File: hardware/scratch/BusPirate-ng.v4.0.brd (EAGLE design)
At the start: 100 x 50 mm, 136 parts, among them CON1 CON-USB-F-MICRO-B, IC10 74LVC1G07DBV, IC11 IC_BUFF_SN74LVC1T45DBV, IC12 74LVC1G07DBV, IC13 IC_BUFF_SN74LVC1T45DBV, IC14 74LVC1G07DBV, IC15 IC_BUFF_SN74LVC1T45DBV, IC16 74LVC1G07DBV, IC17 IC_BUFF_SN74LVC1T45DBV, IC2 IC_MEM_23LC1024, IC3 IC_MEM_23LC1024, IC4 IC_74AC573, IC5 IC_BL1551, IC6 IC_BL1551, IC7 74HCT4066PW, IC8 74LVC1G07DBV, IC9 IC_BUFF_SN74LVC1T45DBV, J1 CON_HEADER_1X04, J2 CON_HEADER_1X03-PTH, J3 CON_HEADER_2X02-PTH, J5 CON_HEADER_1X10-RIGHT_ANGLED_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, U1 IC_FPGA_ICE40HX4K, U2 IC_UC_STM32F103ZX, U3 IC_MEM_AT45DB041D

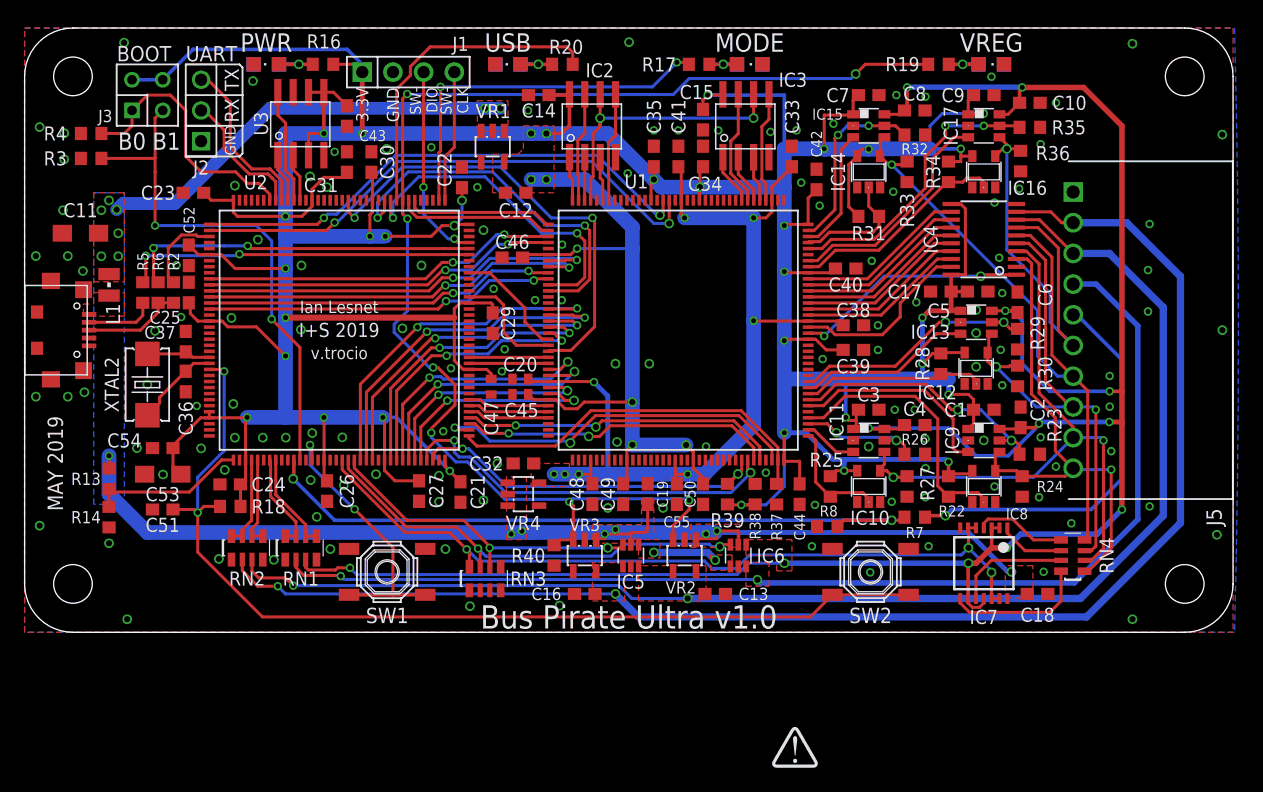
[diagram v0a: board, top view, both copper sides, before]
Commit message: renumber parts
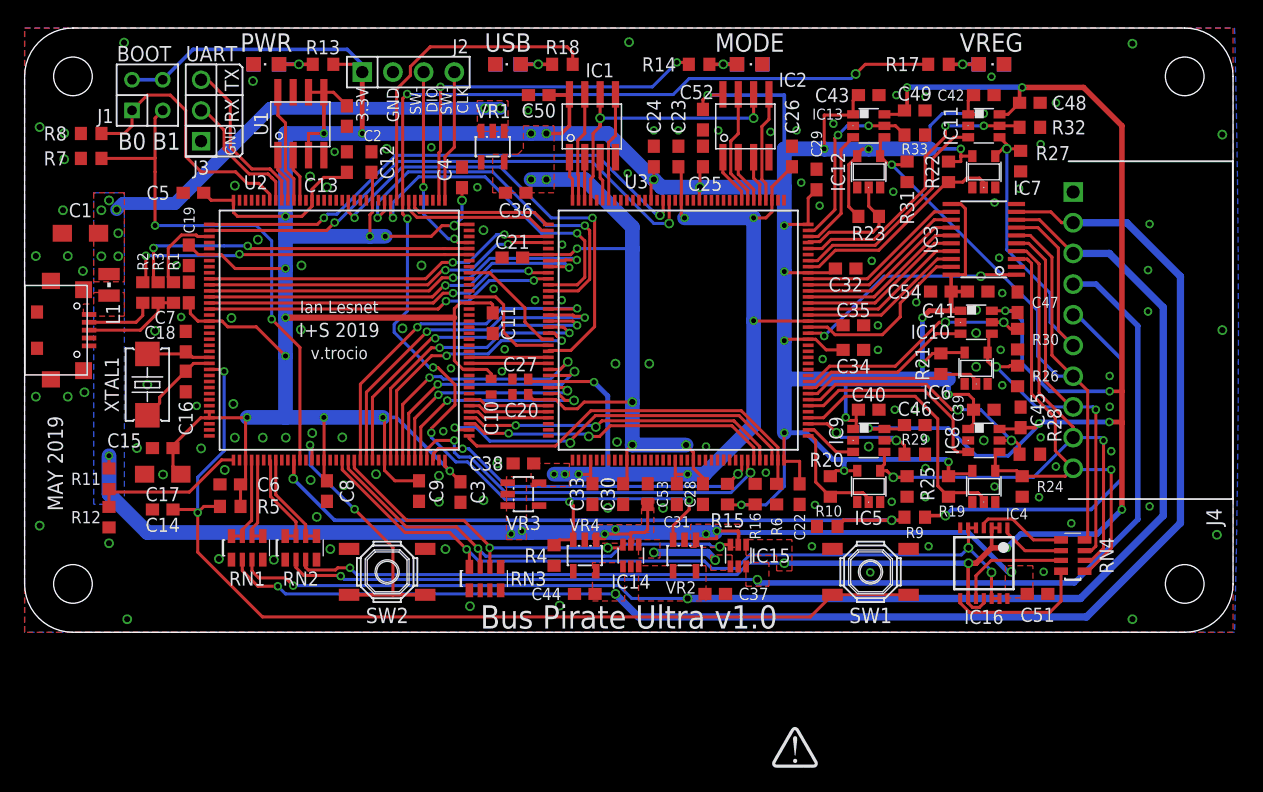
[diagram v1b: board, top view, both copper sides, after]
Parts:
- removed C55: 0.1uF, rcl:C0603
- removed IC17: IC_BUFF_SN74LVC1T45DBV, dp_devices.v6:DBV-R-PDSO-G6
- removed R34, R35: 100K, rcl:R0603
- removed R36: 1M, rcl:R0603
- removed R37, R40: 10K, dp_devices:R603
- removed R38: 10K, rcl:R0603
- added C28: 0.1uF, rcl:C0603
- added IC1: IC_MEM_23LC1024, dp_devices:SOIC-8
- added R1: 1.5K, dp_devices.v6:R603
- added R10, R11, R12, R9: 10K, resistor:R0603
- added R21: 100K, rcl:R0603
- C1: value 0.1uF -> 10uF; device rcl:C0603 -> rcl:SMC_A
- C10, C27: device rcl:C0603 -> dp_devices.v6:C402
- C11: value 10uF -> 0.1uF; device rcl:SMC_A -> rcl:C0603
- C12, C32: value 1uf -> 0.1uF
- C13: value 1uF -> 0.1uF
- C16: value 1uF -> 22pF
- C17: value 0.1uF -> 1uF; device rcl:C0603 -> rcl:SMC_A
- C18: value 0.1uF -> 22pF
- C36: value 22pF -> 1uf
- C37: value 22pF -> 1uF
- C38: value 0.1uF -> 1uf
- C44: value 0.1uF -> 1uF
- C45, C47: device dp_devices.v6:C402 -> rcl:C0603
- C53: value 1uF -> 0.1uF; device rcl:SMC_A -> rcl:C0603
- IC10, IC8: value 74LVC1G07DBV -> IC_BUFF_SN74LVC1T45DBV; device 74xx-little-de:SOT23-5 -> dp_devices.v6:DBV-R-PDSO-G6
- IC14: value 74LVC1G07DBV -> IC_BL1551; device 74xx-little-de:SOT23-5 -> dp_devices.v6:SC-70-6
- IC15: value IC_BUFF_SN74LVC1T45DBV -> IC_BL1551; device dp_devices.v6:DBV-R-PDSO-G6 -> dp_devices.v6:SC-70-6
- IC16: value 74LVC1G07DBV -> 74HCT4066PW; device 74xx-little-de:SOT23-5 -> 40xx:40XX_TSSOP14
- IC3: value IC_MEM_23LC1024 -> IC_74AC573; device dp_devices:SOIC-8 -> dp_devices:TSSOP-20
- IC4: value IC_74AC573 -> 74LVC1G07DBV; device dp_devices:TSSOP-20 -> 74xx-little-de:SOT23-5
- IC5, IC6: value IC_BL1551 -> 74LVC1G07DBV; device dp_devices.v6:SC-70-6 -> 74xx-little-de:SOT23-5
- IC7: value 74HCT4066PW -> 74LVC1G07DBV; device 40xx:40XX_TSSOP14 -> 74xx-little-de:SOT23-5
- J1: value CON_HEADER_1X04 -> CON_HEADER_2X02-PTH; device dp_devices.v6:M1X4 -> dp_devices:M2X2
- J2: value CON_HEADER_1X03-PTH -> CON_HEADER_1X04; device dp_devices.v6:M1X3 -> dp_devices.v6:M1X4
- J3: value CON_HEADER_2X02-PTH -> CON_HEADER_1X03-PTH; device dp_devices:M2X2 -> dp_devices.v6:M1X3
- R13, R14: value 10K -> 1K1; device resistor:R0603 -> dp_devices:R603
- R16: value 1K1 -> 10K; device dp_devices:R603 -> rcl:R0603
- R18: value 10K -> 1K1; device dp_devices.v6:R603 -> dp_devices:R603
- R19, R20: value 1K1 -> 100K; device dp_devices:R603 -> rcl:R0603
- R2: value 1.5K -> 22R
- R25, R26, R31: value 100K -> 1M
- R3: value 10K -> 22R; device rcl:R0603 -> dp_devices.v6:R603
- R30, R33: value 1M -> 100K
- R4: device rcl:R0603 -> dp_devices:R603
- R5: value 22R -> 10K
- R6: value 22R -> 10K; device dp_devices.v6:R603 -> dp_devices:R603
- R7, R8: device resistor:R0603 -> rcl:R0603
- U1: value IC_FPGA_ICE40HX4K -> IC_MEM_AT45DB041D; device dp_devices.v6:TQFP-144 -> dp_devices.v6:SOIC-8
- U3: value IC_MEM_AT45DB041D -> IC_FPGA_ICE40HX4K; device dp_devices.v6:SOIC-8 -> dp_devices.v6:TQFP-144
- VR3: value MCP1801T-5002I/OT -> MCP1801T-1202I/OT
- VR4: value MCP1801T-1202I/OT -> MCP1801T-5002I/OT
- moved C1 76.2 mm to (4.62, 33.0), turned to 180 degrees
- moved R7 74.3 mm to (5.51, 39.2)
- moved C18 73.5 mm to (13.3, 24.1), turned to 270 degrees
- moved C51 72.7 mm to (83.8, 3.17)
- moved R8 69.0 mm to (5.51, 41.3), turned to 180 degrees
- moved C6 66.9 mm to (17.0, 12.2), turned to 0 degrees
- moved C17 66.1 mm to (11.4, 13.1)
- moved C54 65.7 mm to (75.8, 28.2), turned to 180 degrees
- moved C5 65.4 mm to (14.0, 36.4)
- moved R14 61.6 mm to (55.8, 47.0), turned to 180 degrees
- moved C2 61.1 mm to (26.7, 42.7), turned to 90 degrees
- moved C7 58.6 mm to (13.6, 28.1), turned to 270 degrees
- moved C8 57.9 mm to (25.0, 11.7), turned to 90 degrees
- moved C9 57.1 mm to (32.6, 11.7), turned to 90 degrees
- moved R6 53.8 mm to (62.2, 11.4)
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- renumbered J5 to J4, R39 to R15, XTAL2 to XTAL1
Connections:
- net 1V2: now also C23.2, C26.2, C27.1, C31.2, C35.2, C38.1, U3.111, U3.126, U3.27, U3.40, U3.54, U3.92, VR3.5; no longer C20.1, C32.1, C38.2, C41.2, C48.2, C55.2, U1.111, U1.126, U1.27, U1.40, U1.54, U1.92, VR4.5
- net 3V3: now also C10.1, C11.2, C12.2, C13.2, C15.2, C17.+, C19.2, C2.2, C20.1, C28.2, C3.2, C32.2, C36.1, C39.1, C4.2, C40.1, C41.1, C42.1, C43.1, C5.2, C50.1, C52.1, C54.1, C6.2, C7.2, C8.2, C9.2, IC1.8, IC10.1, IC3.11, IC3.20, IC4.5, IC5.5, IC6.5, IC7.5, IC8.1, J1.2, J1.4, J2.1, R13.2, R19.2, R20.2, R21.2, R23.2, R5.2, U1.3, U1.5, U3.100, U3.108, U3.123, U3.131, U3.30, U3.46, U3.57, U3.72, U3.89; no longer C1.1, C12.1, C14.1, C15.1, C17.1, C23.2, C26.2, C27.2, C3.1, C31.2, C35.2, C39.2, C40.2, C42.2, C43.2, C44.2, C45.1, C46.2, C47.1, C49.2, C5.1, C50.2, C52.2, C53.+, C54.2, C7.1, C9.1, IC10.5, IC14.5, IC15.1, IC16.5, IC17.1, IC3.8, IC4.11, IC4.20, IC8.5, J1.1, J3.2, J3.4, R18.2, R25.2, R28.2, R31.2, R34.2, R38.2, U1.100, U1.108, U1.123, U1.131, U1.30, U1.46, U1.57, U1.72, U1.89, U3.3, U3.5
- net ADC1: now also R10.2, R9.2; no longer R7.2, R8.2
- net ADC2: now also RN2.7, RN2.8; no longer RN1.7, RN1.8
- net ADC3: now also RN1.5, RN1.6; no longer RN2.5, RN2.6
- net ADC4: now also RN1.7, RN1.8; no longer RN2.7, RN2.8
- net ADC5: now also R11.2, R12.2; no longer R13.2, R14.2
- net ADC6: now also RN2.5, RN2.6; no longer RN1.5, RN1.6
- net BOOT0: now also J1.1, R8.1; no longer J3.1, R4.1
- net BOOT1: now also J1.3, R7.1; no longer J3.3, R3.1
- net BPIO_AUX: now also IC11.4, IC3.7, IC7.4, R27.2; no longer IC16.4, IC17.4, IC4.7, R36.2
- net BPIO_CLOCK: now also IC3.4, IC5.4, IC9.4, R25.2; no longer IC10.4, IC11.4, IC4.4, R27.2
- net BPIO_CS: now also IC12.4, IC13.4, IC3.6, R31.2; no longer IC14.4, IC15.4, IC4.6, R33.2
- net BPIO_MISO: now also IC10.4, IC3.5, IC6.4, R26.2; no longer IC12.4, IC13.4, IC4.5, R30.2
- net BPIO_MOSI: now also IC3.3, IC4.4; no longer IC4.3, IC9.4
- net BUFDIR_AUX: now also IC11.5, R32.2, U3.104; no longer IC17.5, R35.2, U1.104
- net BUFDIR_CLOCK: now also IC9.5, R29.2, U3.75; no longer IC11.5, R26.2, U1.75
- net BUFDIR_CS: now also IC13.5, R33.2, U3.107; no longer IC15.5, R32.2, U1.107
- net BUFDIR_MISO: now also IC10.5, R30.2, U3.82; no longer IC13.5, R29.2, U1.82
- net BUFDIR_MOSI: now also IC8.5, R28.2, U3.79; no longer IC9.5, R23.2, U1.79
- net BUFIO_AUX: now also IC11.3, U3.102; no longer IC17.3, U1.102
- net BUFIO_CLOCK: now also IC9.3, U3.74; no longer IC11.3, U1.74
- net BUFIO_CS: now also IC13.3, U3.106; no longer IC15.3, U1.106
- net BUFIO_MISO: now also IC10.3, U3.81; no longer IC13.3, U1.81
- net BUFIO_MOSI: now also IC8.3, U3.78; no longer IC9.3, U1.78
- net BUFOD_AUX: now also IC7.2, R22.1, U3.101; no longer IC16.2, R34.1, U1.101
- net BUFOD_CLOCK: now also IC5.2, R20.1, U3.73; no longer IC10.2, R25.1, U1.73
- net BUFOD_CS: now also IC12.2, R23.1, U3.105; no longer IC14.2, R31.1, U1.105
- net BUFOD_MISO: now also IC6.2, R21.1, U3.80; no longer IC12.2, R28.1, U1.80
- net BUFOD_MOSI: now also IC4.2, R19.1, U3.76; no longer IC8.2, R22.1, U1.76
- net D+: now also R1.1, R3.2; no longer R2.1, R6.2
- net D-: now also R2.2; no longer R5.2
- net FLASH_MISO: now also U1.8; no longer U3.8
- net FLASH_MOSI: now also U1.1; no longer U3.1
- net FLASH_SCK: now also U1.2; no longer U3.2
- net FPGA_CDONE: now also U3.65; no longer U1.65
- net FPGA_CRESET: now also R16.1, U3.66; no longer R38.1, U1.66
- net FPGA_PROG_CLOCK: now also U3.70; no longer U1.70
- net FPGA_PROG_CS: now also R6.1, U3.71; no longer R37.1, U1.71
- net FPGA_PROG_MISO: now also U3.67; no longer U1.67
- net FPGA_PROG_MOSI: now also U3.68; no longer U1.68
- net FSMC_A0: now also U3.3; no longer U1.3
- net FSMC_A1: now also U3.4; no longer U1.4
- net FSMC_A2: now also U3.7; no longer U1.7
- net FSMC_A3: now also U3.8; no longer U1.8
- net FSMC_A4: now also U3.9; no longer U1.9
- net FSMC_A5: now also U3.10; no longer U1.10
- net FSMC_D0: now also U3.24; no longer U1.24
- net FSMC_D1: now also U3.23; no longer U1.23
- net FSMC_D10: now also U3.26; no longer U1.26
- net FSMC_D11: now also U3.28; no longer U1.28
- net FSMC_D12: now also U3.29; no longer U1.29
- net FSMC_D13: now also U3.33; no longer U1.33
- net FSMC_D14: now also U3.32; no longer U1.32
- net FSMC_D15: now also U3.31; no longer U1.31
- net FSMC_D2: now also U3.1; no longer U1.1
- net FSMC_D3: now also U3.2; no longer U1.2
- net FSMC_D4: now also U3.15; no longer U1.15
- net FSMC_D5: now also U3.16; no longer U1.16
- net FSMC_D6: now also U3.17; no longer U1.17
- net FSMC_D7: now also U3.18; no longer U1.18
- net FSMC_D8: now also U3.19; no longer U1.19
- net FSMC_D9: now also U3.25; no longer U1.25
- net FSMC_NE3_CE: now also U3.22; no longer U1.22
- net FSMC_NOE_OE: now also U3.11; no longer U1.11
- net FSMC_NWE_WE: now also U3.12; no longer U1.12
- net GND: now also C1.-, C10.2, C11.1, C12.1, C13.1, C14.1, C15.1, C16.1, C17.-, C18.1, C19.1, C27.2, C28.1, C3.1, C32.1, C36.2, C37.2, C38.2, C39.2, C40.2, C41.2, C42.2, C43.2, C44.2, C45.1, C47.1, C5.1, C50.2, C51.2, C52.2, C53.2, C54.2, C7.1, C9.1, IC1.4, IC10.2, IC14.2, IC16.7, IC3.10, IC3.2, IC4.3, IC5.3, IC6.3, IC7.3, IC8.2, J2.2, J3.1, R10.1, R12.1, R25.1, R28.1, R31.1, R6.2, R7.2, R8.2, U1.4, U1.7, U3.103, U3.127, U3.13, U3.132, U3.14, U3.140, U3.5, U3.53, U3.59, U3.69, U3.86; no longer C1.2, C10.1, C11.-, C12.2, C13.2, C14.2, C15.2, C16.2, C17.2, C18.2, C19.2, C27.1, C3.2, C32.2, C36.1, C37.1, C38.1, C39.1, C40.1, C41.1, C42.1, C43.1, C44.1, C45.2, C47.2, C5.2, C50.1, C51.1, C52.1, C53.-, C54.1, C55.1, C7.2, C9.2, IC10.3, IC14.3, IC16.3, IC17.2, IC3.4, IC4.10, IC4.2, IC5.2, IC6.2, IC7.7, IC8.3, J1.2, J2.1, R14.1, R23.1, R3.2, R35.1, R36.1, R37.2, R40.2, R8.1, U1.103, U1.127, U1.13, U1.132, U1.14, U1.140, U1.5, U1.53, U1.59, U1.69, U1.86, U3.4, U3.7
- net IO_ADC/DAC: now also R9.1; no longer R7.1
- net LAT_AUX0: now also IC3.14, U3.97; no longer IC4.14, U1.97
- net LAT_AUX1: now also IC3.19, U3.91; no longer IC4.19, U1.91
- net LAT_CLK: now also IC3.17, U3.94; no longer IC4.17, U1.94
- net LAT_CS: now also IC3.15, U3.96; no longer IC4.15, U1.96
- net LAT_MISO: now also IC3.16, U3.95; no longer IC4.16, U1.95
- net LAT_MOSI: now also IC3.18, U3.93; no longer IC4.18, U1.93
- net LAT_OE: now also IC3.1, U3.90; no longer IC4.1, U1.90
- net LAT_SWV33: now also IC3.13, U3.98; no longer IC4.13, U1.98
- net LAT_SWV50: now also IC3.12, U3.99; no longer IC4.12, U1.99
- net LD1: now also R14.2; no longer R17.2
- net MCU_INT0: now also U3.129; no longer U1.129
- net MCU_INT1: now also U3.128; no longer U1.128
- net MCU_MCO: now also U3.20; no longer U1.20
- net MS0: now also SW2.1, SW2.2; no longer SW1.1, SW1.2
- net N$1: now also IC14.4, IC15.1; no longer IC5.4, IC6.1
- net N$11: now also U3.125; no longer U1.125
- net N$12: now also U3.124; no longer U1.124
- net N$13: now also R18.1; no longer R20.1
- net N$14: now also U3.122; no longer U1.122
- net N$16: now also U3.121; no longer U1.121
- net N$17: now also U3.34; no longer U1.34
- net N$18: now also R17.1; no longer R19.1
- net N$2: now also IC16.1; no longer IC7.1
- net N$20: now also U3.120; no longer U1.120
- net N$24: now also U3.110; no longer U1.110
- net N$26: now also U3.119; no longer U1.119
- net N$3: now also IC16.4; no longer IC7.4
- net N$4: now also IC16.8; no longer IC7.8
- net N$48: now also U3.117; no longer U1.117
- net N$49: now also U3.118; no longer U1.118
- net N$5: now also IC16.10; no longer IC7.10
- net N$6: now also R14.1; no longer R17.1
- net N$7: now also R13.1; no longer R16.1
- net N$8: now also C18.2; no longer C37.2
- net N$9: now also C16.2; no longer C36.2
- net PWM: now also U3.21; no longer U1.21
- net RST: now also C14.2, R5.1, SW1.1, SW1.2; no longer C51.2, R18.1, SW2.1, SW2.2
- net SRAM0_CS: now also IC1.1, U3.144; no longer IC2.1, U1.144
- net SRAM0_SIO0: now also IC1.5, U3.138; no longer IC2.5, U1.138
- net SRAM0_SIO1: now also IC1.2, U3.142; no longer IC2.2, U1.142
- net SRAM0_SIO2: now also IC1.3, U3.139; no longer IC2.3, U1.139
- net SRAM0_SIO3: now also IC1.7, U3.143; no longer IC2.7, U1.143
- net SRAM1_CS: now also IC2.1, U3.116; no longer IC3.1, U1.116
- net SRAM1_SIO0: now also IC2.5, U3.112; no longer IC3.5, U1.112
- net SRAM1_SIO1: now also IC2.2, U3.114; no longer IC3.2, U1.114
- net SRAM1_SIO2: now also IC2.3, U3.113; no longer IC3.3, U1.113
- net SRAM1_SIO3: now also IC2.7, U3.115; no longer IC3.7, U1.115
- net SRAM_CLOCK: now also IC1.6, U3.141; no longer IC3.6, U1.141
- net SWCLK: now also J2.4; no longer J1.4
- net SWDIO: now also J2.3; no longer J1.3
- net SWV33: now also C37.1, IC14.3, IC3.8, RN1.3; no longer C13.1, IC4.8, IC5.3, RN2.3
- net SWV50: now also C44.1, IC14.1, IC3.9, RN1.2, VR4.5; no longer C16.1, IC4.9, IC5.1, RN2.2, VR3.5
- net UART_RX: now also J3.2; no longer J2.2
- net UART_TX: now also J3.3; no longer J2.3
- net USBLED: now also R18.2; no longer R20.2
- net USB_D+: now also R3.1; no longer R6.1
- net USB_D-: now also R2.1; no longer R5.1
- net USB_DET: now also R1.2; no longer R2.2
- net V33PU: now also IC15.6; no longer IC6.6
- net V50PU: now also IC14.6; no longer IC5.6
- net VEXTERN: now also IC15.3, RN2.2; no longer IC6.3, RN1.2
- net VEXTPU: now also IC16.12, IC16.13, IC16.5, IC16.6; no longer IC7.12, IC7.13, IC7.5, IC7.6
- net VPP_FAST: now also U3.109; no longer U1.109
- net VPUN: now also C45.2, C46.2, C47.2, C48.2, C49.2, IC10.6, IC15.4, IC16.11, IC16.2, IC16.3, IC16.9, IC8.6, RN2.3; no longer C10.2, C2.2, C4.2, C6.2, C8.2, IC15.6, IC17.6, IC6.4, IC7.11, IC7.2, IC7.3, IC7.9, RN1.3
- net VREGEN: now also R17.2, R4.1, VR4.3; no longer R19.2, R40.1, VR3.3
- net VUSB: now also C1.+, C51.1, C53.1, IC14.5, IC15.5, IC16.14, R11.1, VR3.3; no longer C11.+, C18.1, C19.1, IC5.5, IC6.5, IC7.14, R13.1, VR4.3

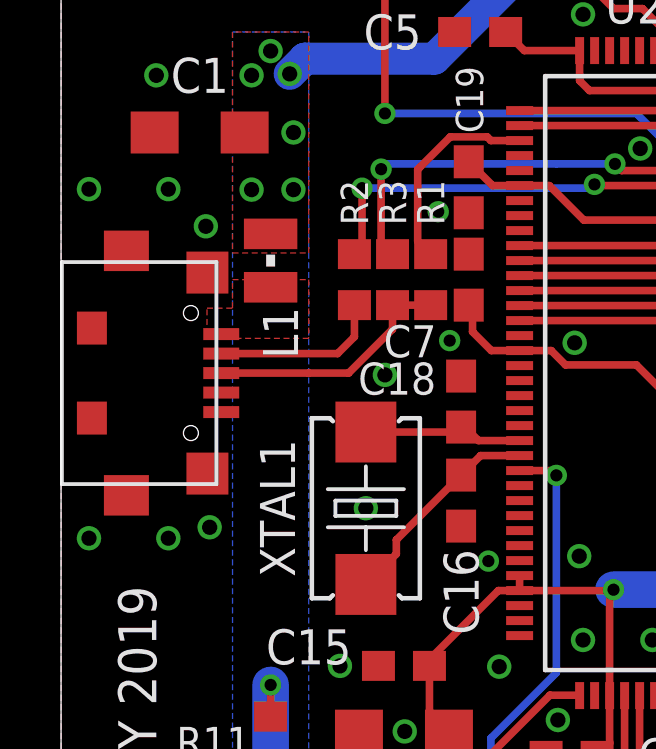
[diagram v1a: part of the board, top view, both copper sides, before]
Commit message: replaced USB mini-B connector, fix DRC errors on the said connector
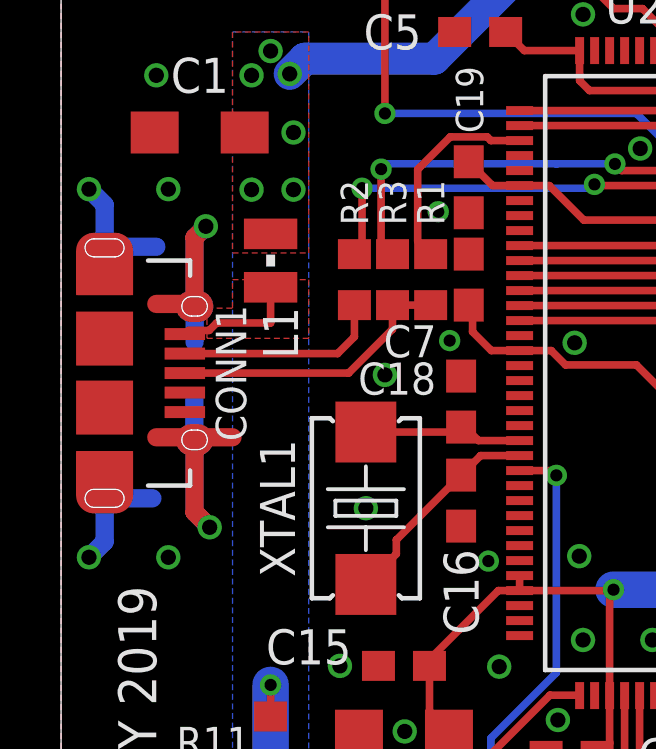
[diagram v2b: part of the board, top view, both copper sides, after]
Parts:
- removed CON1: CON-USB-F-MICRO-B, dp_devices.v6:CON_USB_MICRO-B-1-MD05SMXXX-01
- added CONN1: CON-USB-F-MICRO-B-2, dp_devices.v6:CON_USB_MICRO-B-2-SD-47589-001
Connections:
- net D+: now also CONN1.P3; no longer CON1.P3
- net D-: now also CONN1.P2; no longer CON1.P2
- net EXVUSB: now also CONN1.P1; no longer CON1.P1
- net GND: now also CONN1.BODY@1, CONN1.BODY@10, CONN1.BODY@2, CONN1.BODY@3, CONN1.BODY@4, CONN1.BODY@5, CONN1.BODY@6, CONN1.BODY@7, CONN1.BODY@8, CONN1.BODY@9, CONN1.P5; no longer CON1.GND1, CON1.GND2, CON1.GND3, CON1.GND4, CON1.GND5, CON1.GND6, CON1.P5
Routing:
- net GND: track 0.44 -> 28.8 mm
- net EXVUSB: track 0.00 -> 4.20 mm
- net D-: track 5.73 -> 6.94 mm
- net D+: track 8.39 -> 9.60 mm
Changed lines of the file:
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@@
 <setting verticaltext="up"/>
 </settings>
-<grid distance="25" unitdist="mil" unit="mil" style="lines" multiple="1" display="no" altdistance="1" altunitdist="mil" altunit="mil"/>
+<grid distance="25" unitdist="mil" unit="mil" style="lines" multiple="1" display="no" altdistance="5" altunitdist="mil" altunit="mil"/>
 <layers>
 <layer number="1" name="Top" color="4" fill="1" visible="yes" active="yes"/>
@@
 <wire x1="13.335" y1="44.45" x2="18.034" y2="44.45" width="0.1524" layer="21"/>
 <text x="80" y="48.8" size="1.524" layer="22" font="vector" ratio="15" rot="MR180" align="center">VREG</text>
+<polygon width="0.1524" layer="41">
+<vertex x="0.762" y="20.701"/>
+<vertex x="2.159" y="20.701"/>
+<vertex x="2.159" y="20.066"/>
+<vertex x="0.762" y="20.066"/>
+</polygon>
+<polygon width="0.1524" layer="41">
+<vertex x="0.762" y="29.845"/>
+<vertex x="2.159" y="29.845"/>
+<vertex x="2.159" y="29.21"/>
+<vertex x="0.762" y="29.21"/>
+</polygon>
+<polygon width="0.1524" layer="41">
+<vertex x="3.81" y="22.987"/>
+<vertex x="5.08" y="22.987"/>
+<vertex x="5.08" y="22.352"/>
+<vertex x="3.81" y="22.352"/>
+</polygon>
+<polygon width="0.1524" layer="41">
+<vertex x="3.81" y="27.686"/>
+<vertex x="5.08" y="27.686"/>
+<vertex x="5.08" y="27.051"/>
+<vertex x="3.81" y="27.051"/>
+</polygon>
+<polygon width="0.1524" layer="42">
+<vertex x="3.81" y="27.686"/>
+<vertex x="5.08" y="27.686"/>
+<vertex x="5.08" y="26.67"/>
+<vertex x="3.81" y="26.67"/>
+</polygon>
+<polygon width="0.1524" layer="42">
+<vertex x="3.81" y="23.241"/>
+<vertex x="5.08" y="23.241"/>
+<vertex x="5.08" y="22.352"/>
+<vertex x="3.81" y="22.352"/>
+</polygon>
 </plain>
 <attributes>
@@
 <attribute name="VALUE" x="36.1" y="1.445" size="1.27" layer="27" font="vector"/>
 </element>
-<element name="CON1" library="dp_devices.v6" package="CON_USB_MICRO-B-1-MD05SMXXX-01" value="CON-USB-F-MICRO-B" x="2.17805" y="25" locked="yes" rot="R270"/>
 <element name="IC15" library="dp_devices.v6" package="SC-70-6" value="IC_BL1551" x="59.055" y="6.35" smashed="yes">
 <attribute name="NAME" x="61.7474" y="6.35" size="1.1684" layer="25" font="vector" ratio="12" align="center"/>
@@
 <attribute name="VALUE" x="36.3855" y="21.59" size="1.27" layer="27" ratio="10" rot="R270"/>
 </element>
+<element name="CONN1" library="dp_devices.v6" package="CON_USB_MICRO-B-2-SD-47589-001" value="CON-USB-F-MICRO-B-2" x="1.1" y="25" rot="R270"/>
 </elements>
 <signals>
@@
 <contactref element="IC3" pad="10"/>
 <contactref element="C54" pad="2"/>
-<via x="0.930275" y="19.494875" extent="1-16" drill="0.508"/>
+<via x="0.930275" y="18.859875" extent="1-16" drill="0.508"/>
 <via x="99.1121" y="41.1833" extent="1-16" drill="0.508"/>
 <via x="99.1121" y="25.0035" extent="1-16" drill="0.508"/>
@@
 <vertex x="0" y="0"/>
 </polygon>
-<via x="3.57505" y="19.494875" extent="1-16" drill="0.508"/>
+<via x="3.57505" y="18.859875" extent="1-16" drill="0.508"/>
 <contactref element="R10" pad="1"/>
 <contactref element="SW2" pad="3"/>
@@
 <contactref element="RN3" pad="2"/>
 <contactref element="RN3" pad="1"/>
-<contactref element="CON1" pad="P5"/>
-<contactref element="CON1" pad="GND6"/>
-<contactref element="CON1" pad="GND1"/>
-<contactref element="CON1" pad="GND2"/>
-<contactref element="CON1" pad="GND3"/>
-<contactref element="CON1" pad="GND4"/>
-<contactref element="CON1" pad="GND5"/>
 <contactref element="IC3" pad="2"/>
 <contactref element="R7" pad="2"/>
@@
 <via x="86.614" y="9.017" extent="1-16" drill="0.4064"/>
 <via x="37.465" y="36.83" extent="1-16" drill="0.4064"/>
+<contactref element="CONN1" pad="P5"/>
+<contactref element="CONN1" pad="BODY@1"/>
+<contactref element="CONN1" pad="BODY@2"/>
+<contactref element="CONN1" pad="BODY@4"/>
+<contactref element="CONN1" pad="BODY@3"/>
+<contactref element="CONN1" pad="BODY@5"/>
+<contactref element="CONN1" pad="BODY@6"/>
+<contactref element="CONN1" pad="BODY@7"/>
+<contactref element="CONN1" pad="BODY@8"/>
+<contactref element="CONN1" pad="BODY@10"/>
+<contactref element="CONN1" pad="BODY@9"/>
+<wire x1="0.930275" y1="31.13125" x2="1.45" y2="30.611525" width="0.6096" layer="16"/>
+<wire x1="1.45" y1="30.611525" x2="1.45" y2="29.175" width="0.6096" layer="16"/>
+<wire x1="4.45" y1="27.225" x2="4.45" y2="29.517" width="0.6096" layer="16"/>
+<wire x1="4.45" y1="29.517" x2="4.826" y2="29.893" width="0.6096" layer="16"/>
+<wire x1="4.45" y1="27.225" x2="4.45" y2="29.517" width="0.6096" layer="1"/>
+<wire x1="4.45" y1="29.517" x2="4.826" y2="29.893" width="0.6096" layer="1"/>
+<wire x1="1.45" y1="20.825" x2="1.45" y2="19.3796" width="0.6096" layer="16"/>
+<wire x1="1.45" y1="19.3796" x2="0.930275" y2="18.859875" width="0.6096" layer="16"/>
+<wire x1="4.45" y1="22.775" x2="4.45" y2="20.363" width="0.6096" layer="1"/>
+<wire x1="4.45" y1="20.363" x2="4.953" y2="19.86" width="0.6096" layer="1"/>
+<wire x1="4.45" y1="22.775" x2="4.45" y2="20.363" width="0.6096" layer="16"/>
+<wire x1="4.45" y1="20.363" x2="4.953" y2="19.86" width="0.6096" layer="16"/>
+<wire x1="1.45" y1="29.175" x2="1.45" y2="28.12" width="0.6096" layer="16"/>
+<wire x1="1.45" y1="29.175" x2="1.485" y2="29.21" width="0.6096" layer="16"/>
+<wire x1="1.485" y1="29.21" x2="3.175" y2="29.21" width="0.6096" layer="16"/>
+<wire x1="1.45" y1="20.825" x2="1.45" y2="22.045" width="0.6096" layer="16"/>
+<wire x1="1.45" y1="20.825" x2="3.045" y2="20.825" width="0.6096" layer="16"/>
+<wire x1="4.45" y1="22.775" x2="4.445" y2="22.78" width="0.6096" layer="16"/>
+<wire x1="4.445" y1="22.78" x2="4.445" y2="24.13" width="0.6096" layer="16"/>
+<wire x1="4.45" y1="27.225" x2="4.45" y2="26.04" width="0.6096" layer="16"/>
+<wire x1="4.45" y1="22.775" x2="4.535" y2="22.86" width="0.6096" layer="1"/>
+<wire x1="4.535" y1="22.86" x2="5.715" y2="22.86" width="0.6096" layer="1"/>
+<wire x1="4.45" y1="22.775" x2="4.365" y2="22.86" width="0.6096" layer="1"/>
+<wire x1="4.365" y1="22.86" x2="3.175" y2="22.86" width="0.6096" layer="1"/>
+<wire x1="4.45" y1="27.225" x2="4.37" y2="27.305" width="0.6096" layer="1"/>
+<wire x1="4.37" y1="27.305" x2="3.175" y2="27.305" width="0.6096" layer="1"/>
 </signal>
 <signal name="3V3">
@@
 <vertex x="4.864225" y="26.284725"/>
 </polygon>
-<contactref element="CON1" pad="P1"/>
+<contactref element="CONN1" pad="P1"/>
+<wire x1="4.125" y1="26.3" x2="4.2456" y2="26.4206" width="0.254" layer="1"/>
+<wire x1="5.1838125" y1="26.67" x2="6.985" y2="26.67" width="0.254" layer="1"/>
+<wire x1="4.2456" y1="26.4206" x2="4.9344125" y2="26.4206" width="0.254" layer="1"/>
+<wire x1="4.9344125" y1="26.4206" x2="5.1838125" y2="26.67" width="0.254" layer="1"/>
+<wire x1="6.985" y1="26.67" x2="6.985" y2="27.86" width="0.254" layer="1"/>
 </signal>
 <signal name="N$13">
@@
 <signal name="D+">
 <contactref element="R1" pad="1"/>
-<contactref element="CON1" pad="P3"/>
 <contactref element="R3" pad="2"/>
-<wire x1="5.33805" y1="25" x2="8.255" y2="25" width="0.254" layer="1"/>
-<wire x1="8.255" y1="25" x2="9.585" y2="25" width="0.254" layer="1"/>
 <wire x1="9.585" y1="25" x2="11.049" y2="26.464" width="0.254" layer="1"/>
 <wire x1="11.049" y1="26.464" x2="11.049" y2="27.265" width="0.254" layer="1"/>
 <wire x1="11.049" y1="27.265" x2="12.319" y2="27.265" width="0.254" layer="1"/>
+<contactref element="CONN1" pad="P3"/>
+<wire x1="4.125" y1="25" x2="9.585" y2="25" width="0.254" layer="1"/>
 </signal>
 <signal name="D-">
-<contactref element="CON1" pad="P2"/>
 <contactref element="R2" pad="2"/>
-<wire x1="5.33805" y1="25.65" x2="9.219" y2="25.65" width="0.254" layer="1"/>
 <wire x1="9.219" y1="25.65" x2="9.779" y2="26.21" width="0.254" layer="1"/>
 <wire x1="9.779" y1="26.21" x2="9.779" y2="27.265" width="0.254" layer="1"/>
+<contactref element="CONN1" pad="P2"/>
+<wire x1="4.125" y1="25.65" x2="9.219" y2="25.65" width="0.254" layer="1"/>
 </signal>
 <signal name="USB_DET">
@@
 <mfgpreviewcolor name="substratecolor" color="0xFF786E46"/>
 </mfgpreviewcolors>
+<errors>
+</errors>
 </board>
 </drawing>
